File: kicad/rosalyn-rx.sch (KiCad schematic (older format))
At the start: 36 parts, among them J2 Serial1, J3 Serial2, J4 PWM, U1 STM32F303CCTx, U2 E22-EBYTE, U3 XC6206P330MR, U4 TXS0108EPW, U5 BMP280, U6 ICM-20602

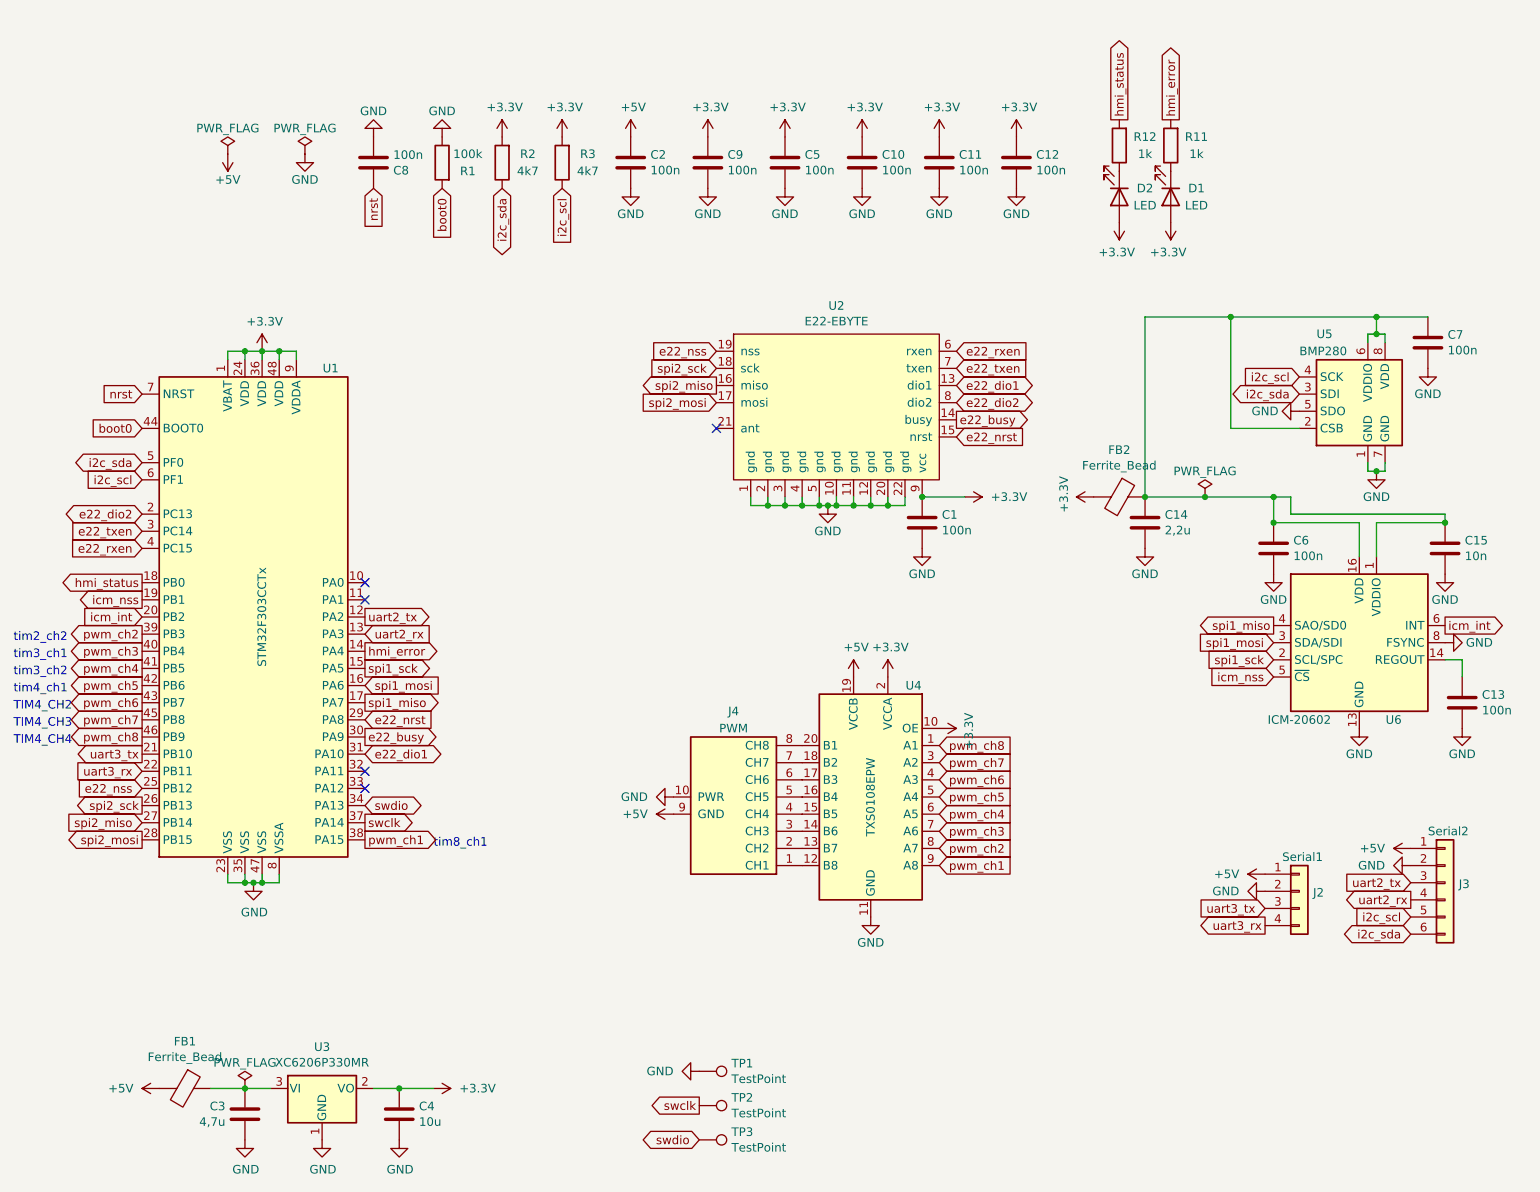
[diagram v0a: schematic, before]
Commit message: added nvdata driver
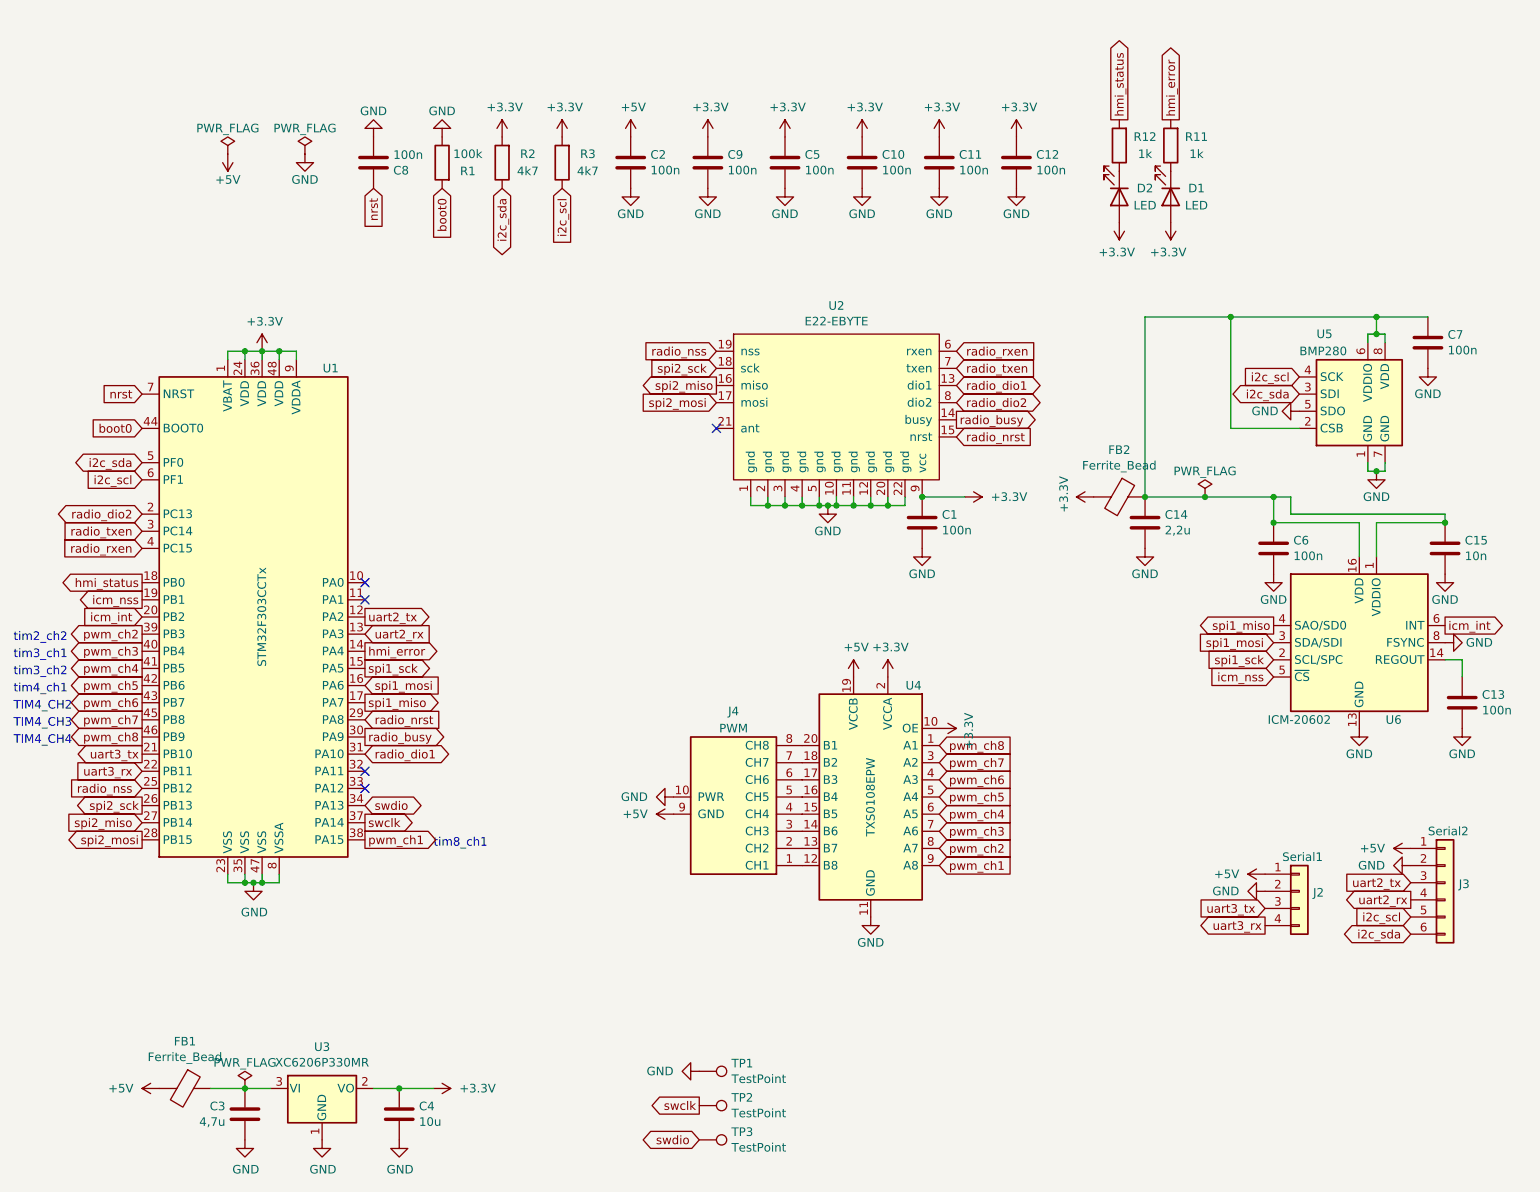
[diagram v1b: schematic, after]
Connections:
- net e22_busy renamed radio_busy
- net e22_dio1 renamed radio_dio1
- net e22_dio2 renamed radio_dio2
- net e22_nrst renamed radio_nrst
- net e22_nss renamed radio_nss
- net e22_rxen renamed radio_rxen
- net e22_txen renamed radio_txen
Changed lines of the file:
@@
 NoConn ~ 6000 3100
 Text GLabel 6000 2650 0    50   Input ~ 0
-e22_nss
+radio_nss
 Text GLabel 6000 2750 0    50   Input ~ 0
 spi2_sck
@@
 spi2_mosi
 Text GLabel 7400 2650 2    50   Input ~ 0
-e22_rxen
+radio_rxen
 Text GLabel 7400 2750 2    50   Input ~ 0
-e22_txen
+radio_txen
 Text GLabel 7400 2850 2    50   BiDi ~ 0
-e22_dio1
+radio_dio1
 Text GLabel 7400 2950 2    50   BiDi ~ 0
-e22_dio2
+radio_dio2
 Text GLabel 7400 3050 2    50   Output ~ 0
-e22_busy
+radio_busy
 Text GLabel 7400 3150 2    50   Input ~ 0
-e22_nrst
+radio_nrst
 Text GLabel 3950 4500 2    50   Output ~ 0
 spi1_sck
@@
 spi2_mosi
 Text GLabel 2650 5200 0    50   Input ~ 0
-e22_nss
+radio_nss
 Text GLabel 3950 4800 2    50   Input ~ 0
-e22_nrst
+radio_nrst
 Text GLabel 3950 4900 2    50   Output ~ 0
-e22_busy
+radio_busy
 Text GLabel 3950 5000 2    50   BiDi ~ 0
-e22_dio1
+radio_dio1
 Text GLabel 2650 3600 0    50   BiDi ~ 0
-e22_dio2
+radio_dio2
 Text GLabel 2650 3700 0    50   Input ~ 0
-e22_txen
+radio_txen
 Text GLabel 2650 3800 0    50   Input ~ 0
-e22_rxen
+radio_rxen
 Text GLabel 9250 4550 0    50   Input ~ 0
 icm_nss
